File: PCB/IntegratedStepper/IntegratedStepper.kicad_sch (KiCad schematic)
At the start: 0 parts

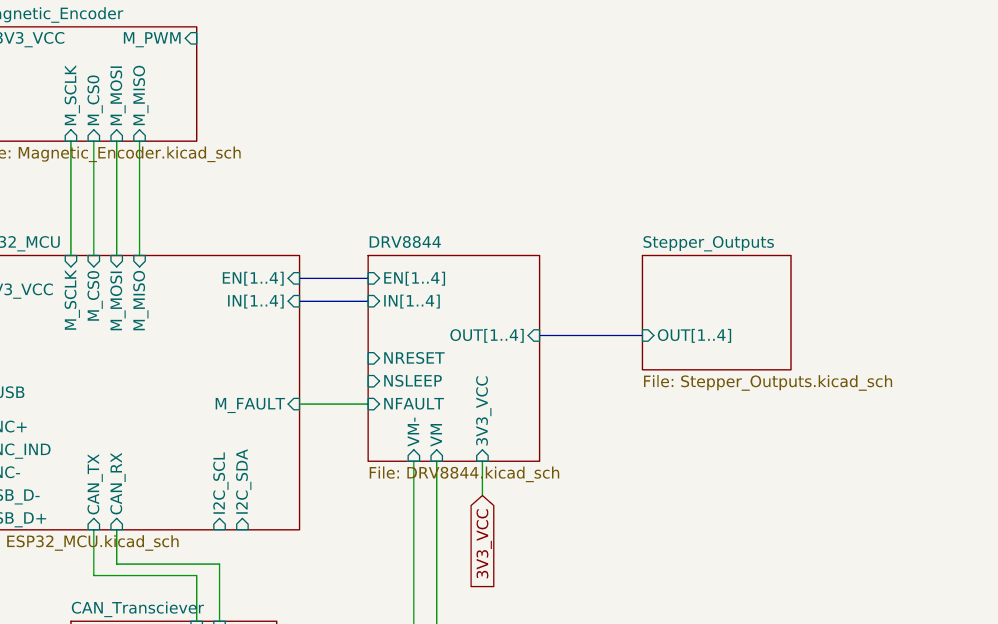
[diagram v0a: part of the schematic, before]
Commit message: Update PCB with DRV8243 for 12A capacity
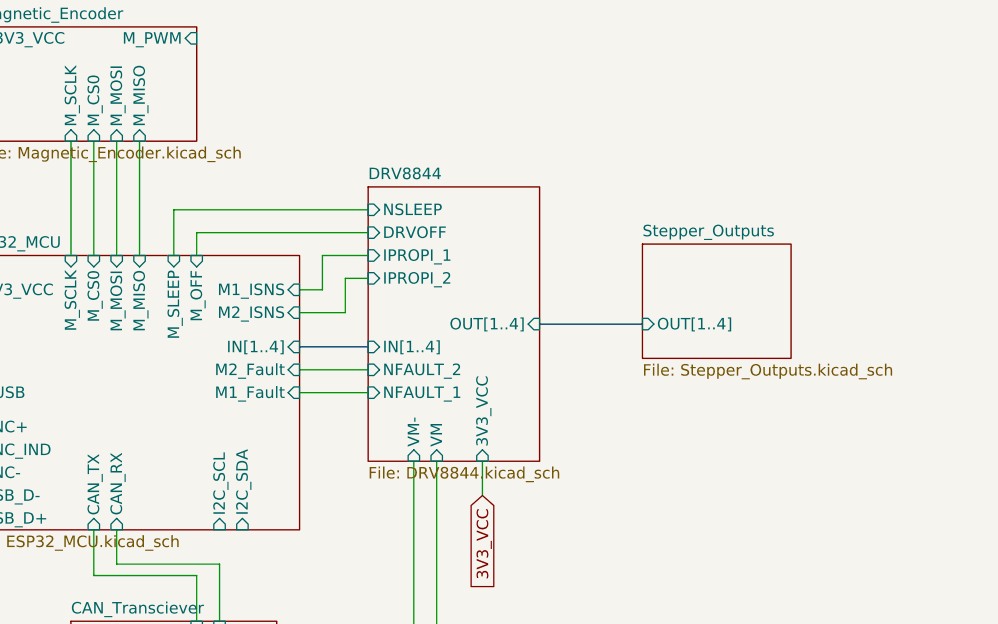
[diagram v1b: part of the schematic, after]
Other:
- sheet DRV8844 ports: added DRVOFF, IPROPI_1, IPROPI_2, NFAULT_1, NFAULT_2; removed EN[1..4], NFAULT, NRESET
- sheet ESP32_MCU ports: added M1_Fault, M1_ISNS, M2_Fault, M2_ISNS, M_OFF, M_SLEEP; removed EN[1..4], M_FAULT

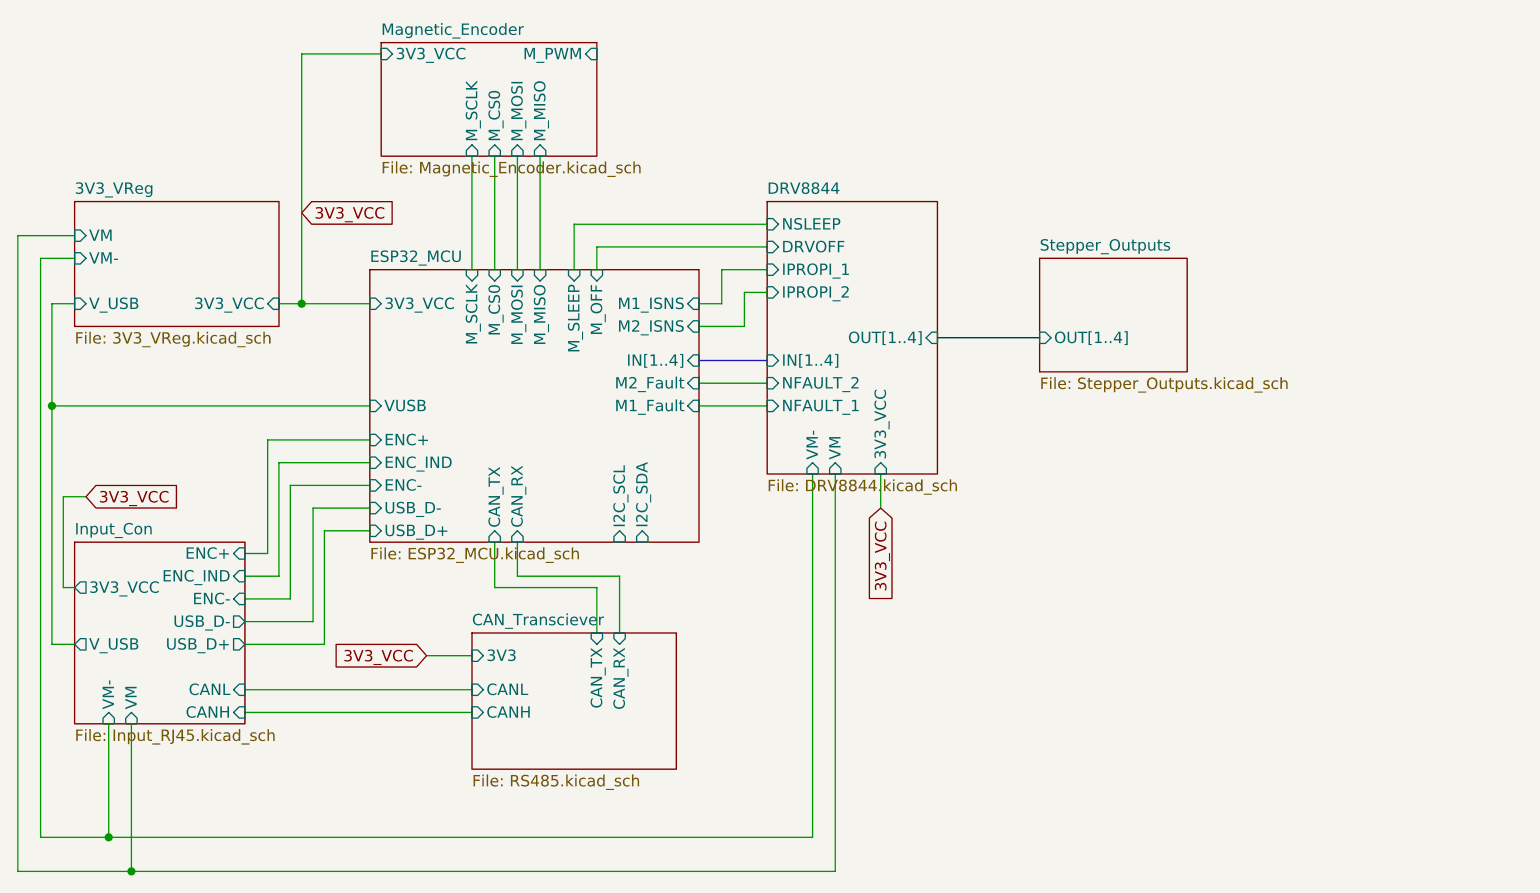
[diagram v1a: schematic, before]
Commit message: update new tester board sch
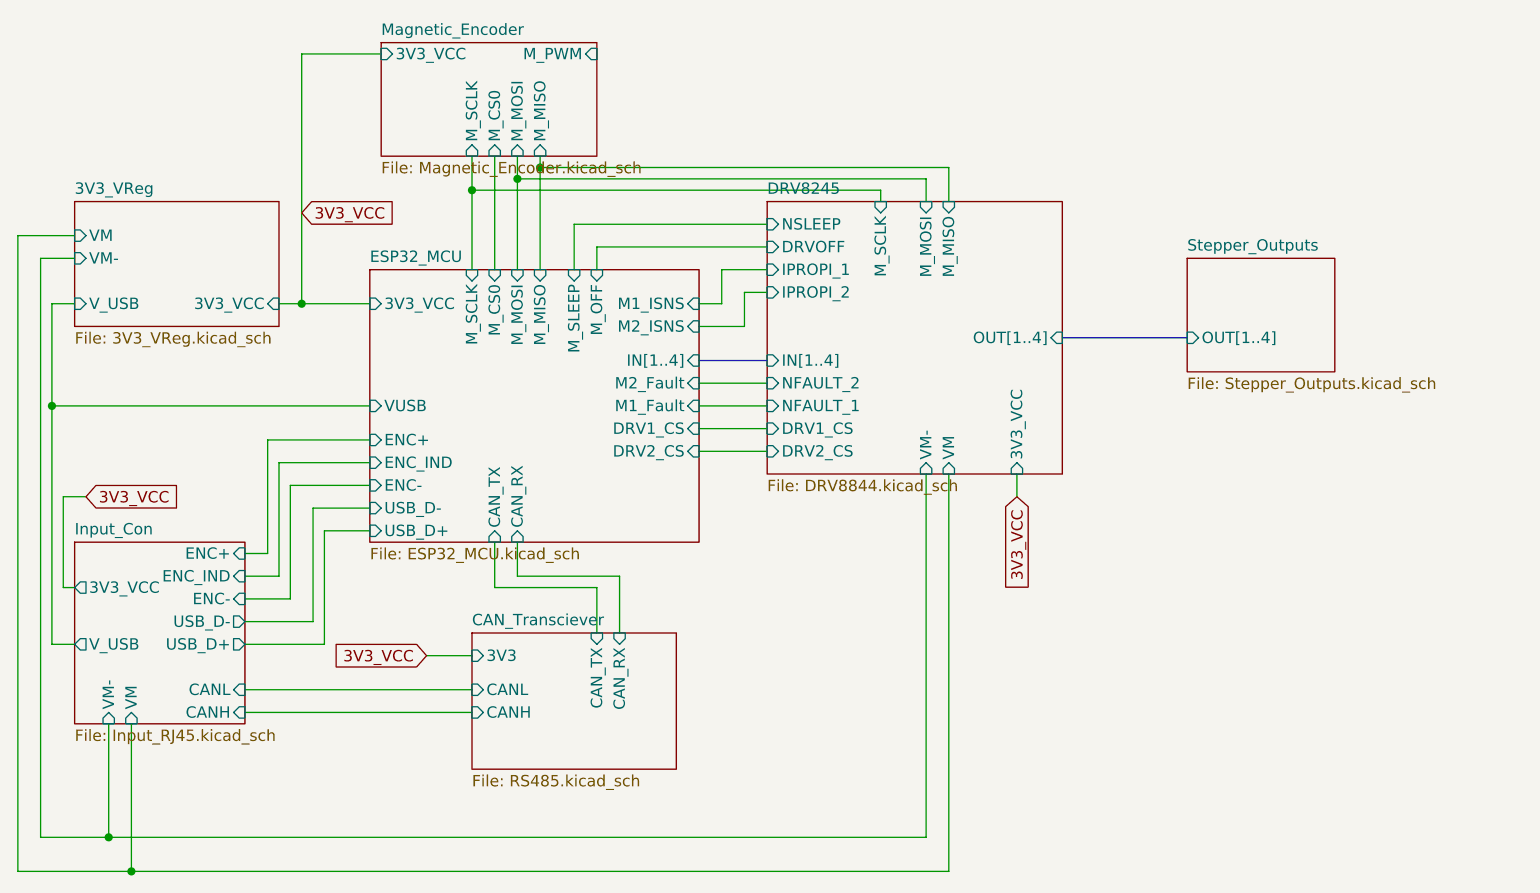
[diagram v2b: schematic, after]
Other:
- sheet DRV8844 renamed DRV8245
- sheet DRV8245 ports: added DRV1_CS, DRV2_CS, M_MISO, M_MOSI, M_SCLK; removed none
- sheet ESP32_MCU ports: added DRV1_CS, DRV2_CS; removed I2C_SCL, I2C_SDA
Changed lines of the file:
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@@
 	(paper "A4")
+	(junction
+		(at 123.19 59.69)
+		(diameter 0)
+		(color 0 0 0 0)
+	)
+	(junction
+		(at 115.57 62.23)
+		(diameter 0)
+		(color 0 0 0 0)
+	)
 	(junction
 		(at 77.47 138.43)
@@
 	)
 	(junction
+		(at 120.65 60.96)
+		(diameter 0)
+		(color 0 0 0 0)
+	)
+	(junction
 		(at 96.52 74.93)
 		(diameter 0)
@@
 	(wire
 		(pts
+			(xy 115.57 62.23) (xy 161.29 62.23)
+		)
+		(stroke
+			(width 0)
+			(type default)
+		)
+	)
+	(wire
+		(pts
 			(xy 129.54 68.58) (xy 148.59 68.58)
 		)
@@
 	(wire
 		(pts
+			(xy 120.65 58.42) (xy 120.65 60.96)
+		)
+		(stroke
+			(width 0)
+			(type default)
+		)
+	)
+	(wire
+		(pts
+			(xy 166.37 60.96) (xy 120.65 60.96)
+		)
+		(stroke
+			(width 0)
+			(type default)
+		)
+	)
+	(wire
+		(pts
 			(xy 93.98 74.93) (xy 96.52 74.93)
 		)
@@
 	(wire
 		(pts
-			(xy 123.19 58.42) (xy 123.19 71.12)
+			(xy 123.19 58.42) (xy 123.19 59.69)
 		)
 		(stroke
@@
 	(wire
 		(pts
+			(xy 140.97 91.44) (xy 148.59 91.44)
+		)
+		(stroke
+			(width 0)
+			(type default)
+		)
+	)
+	(wire
+		(pts
 			(xy 143.51 71.12) (xy 148.59 71.12)
 		)
@@
 	(wire
 		(pts
-			(xy 77.47 138.43) (xy 156.21 138.43)
+			(xy 77.47 138.43) (xy 168.91 138.43)
+		)
+		(stroke
+			(width 0)
+			(type default)
+		)
+	)
+	(wire
+		(pts
+			(xy 168.91 59.69) (xy 123.19 59.69)
 		)
 		(stroke
@@
 		)
 	)
-	(wire
-		(pts
-			(xy 115.57 58.42) (xy 115.57 71.12)
-		)
-		(stroke
-			(width 0)
-			(type default)
-		)
-	)
 	(bus
 		(pts
-			(xy 167.64 78.74) (xy 179.07 78.74)
+			(xy 181.61 78.74) (xy 195.58 78.74)
+		)
+		(stroke
+			(width 0)
+			(type default)
+		)
+	)
+	(wire
+		(pts
+			(xy 115.57 58.42) (xy 115.57 62.23)
 		)
 		(stroke
@@
 	(wire
 		(pts
+			(xy 115.57 62.23) (xy 115.57 71.12)
+		)
+		(stroke
+			(width 0)
+			(type default)
+		)
+	)
+	(wire
+		(pts
 			(xy 68.58 86.36) (xy 68.58 113.03)
 		)
@@
 	(wire
 		(pts
+			(xy 120.65 60.96) (xy 120.65 71.12)
+		)
+		(stroke
+			(width 0)
+			(type default)
+		)
+	)
+	(wire
+		(pts
 			(xy 104.14 92.71) (xy 93.98 92.71)
 		)
@@
 	(wire
 		(pts
-			(xy 153.67 134.62) (xy 153.67 93.98)
+			(xy 166.37 134.62) (xy 166.37 93.98)
 		)
 		(stroke
@@
 	(wire
 		(pts
-			(xy 74.93 134.62) (xy 153.67 134.62)
+			(xy 161.29 62.23) (xy 161.29 63.5)
+		)
+		(stroke
+			(width 0)
+			(type default)
+		)
+	)
+	(wire
+		(pts
+			(xy 140.97 88.9) (xy 148.59 88.9)
+		)
+		(stroke
+			(width 0)
+			(type default)
+		)
+	)
+	(wire
+		(pts
+			(xy 74.93 134.62) (xy 166.37 134.62)
 		)
 		(stroke
@@
 	(wire
 		(pts
-			(xy 156.21 138.43) (xy 156.21 93.98)
-		)
-		(stroke
-			(width 0)
-			(type default)
-		)
-	)
-	(wire
-		(pts
-			(xy 161.29 93.98) (xy 161.29 97.79)
+			(xy 168.91 138.43) (xy 168.91 93.98)
+		)
+		(stroke
+			(width 0)
+			(type default)
+		)
+	)
+	(wire
+		(pts
+			(xy 176.53 93.98) (xy 176.53 96.52)
 		)
 		(stroke
@@
 	(wire
 		(pts
+			(xy 168.91 63.5) (xy 168.91 59.69)
+		)
+		(stroke
+			(width 0)
+			(type default)
+		)
+	)
+	(wire
+		(pts
 			(xy 93.98 105.41) (xy 90.17 105.41)
 		)
@@
 	(wire
 		(pts
-			(xy 120.65 58.42) (xy 120.65 71.12)
+			(xy 123.19 59.69) (xy 123.19 71.12)
+		)
+		(stroke
+			(width 0)
+			(type default)
+		)
+	)
+	(wire
+		(pts
+			(xy 166.37 63.5) (xy 166.37 60.96)
 		)
 		(stroke
@@
 	(global_label "3V3_VCC"
 		(shape input)
-		(at 161.29 97.79 270)
+		(at 176.53 96.52 270)
 		(fields_autoplaced yes)
 		(effects
@@
 		)
 		(property "Intersheetrefs" "${INTERSHEET_REFS}"
-			(at 161.29 108.879 90)
+			(at 176.53 107.609 90)
 			(effects
 				(font
@@
 	)
 	(sheet
-		(at 179.07 69.85)
+		(at 195.58 69.85)
 		(size 16.51 12.7)
 		(fields_autoplaced yes)
@@
 		)
 		(property "Sheetname" "Stepper_Outputs"
-			(at 179.07 69.1384 0)
+			(at 195.58 69.1384 0)
 			(effects
 				(font
@@
 		)
 		(property "Sheetfile" "Stepper_Outputs.kicad_sch"
-			(at 179.07 83.1346 0)
+			(at 195.58 83.1346 0)
 			(effects
 				(font
@@
 		)
 		(pin "OUT[1..4]" input
-			(at 179.07 78.74 180)
+			(at 195.58 78.74 180)
 			(effects
 				(font
@@
 	(sheet
 		(at 148.59 63.5)
-		(size 19.05 30.48)
+		(size 33.02 30.48)
 		(fields_autoplaced yes)
 		(stroke
@@
 			(color 0 0 0 0.0000)
 		)
-		(property "Sheetname" "DRV8844"
+		(property "Sheetname" "DRV8245"
 			(at 148.59 62.7884 0)
 			(effects
@@
 		)
 		(pin "VM-" input
-			(at 153.67 93.98 270)
+			(at 166.37 93.98 270)
 			(effects
 				(font
@@
 		)
 		(pin "VM" input
-			(at 156.21 93.98 270)
+			(at 168.91 93.98 270)
 			(effects
 				(font
@@
 		)
 		(pin "OUT[1..4]" input
-			(at 167.64 78.74 0)
+			(at 181.61 78.74 0)
 			(effects
 				(font
@@
 		)
 		(pin "3V3_VCC" input
-			(at 161.29 93.98 270)
+			(at 176.53 93.98 270)
 			(effects
 				(font
@@
 		(pin "DRVOFF" input
 			(at 148.59 68.58 180)
+			(effects
+				(font
+					(size 1.27 1.27)
+				)
+				(justify left)
+			)
+		)
+		(pin "M_SCLK" input
+			(at 161.29 63.5 90)
+			(effects
+				(font
+					(size 1.27 1.27)
+				)
+				(justify right)
+			)
+		)
+		(pin "M_MISO" input
+			(at 168.91 63.5 90)
+			(effects
+				(font
+					(size 1.27 1.27)
+				)
+				(justify right)
+			)
+		)
+		(pin "M_MOSI" input
+			(at 166.37 63.5 90)
+			(effects
+				(font
+					(size 1.27 1.27)
+				)
+				(justify right)
+			)
+		)
+		(pin "DRV1_CS" input
+			(at 148.59 88.9 180)
+			(effects
+				(font
+					(size 1.27 1.27)
+				)
+				(justify left)
+			)
+		)
+		(pin "DRV2_CS" input
+			(at 148.59 91.44 180)
 			(effects
 				(font
@@
 			)
 		)
-		(pin "I2C_SCL" input
-			(at 132.08 101.6 270)
-			(effects
-				(font
-					(size 1.27 1.27)
-				)
-				(justify left)
-			)
-		)
 		(pin "ENC+" input
 			(at 104.14 90.17 180)
@@
 			)
 		)
-		(pin "I2C_SDA" input
-			(at 134.62 101.6 270)
-			(effects
-				(font
-					(size 1.27 1.27)
-				)
-				(justify left)
-			)
-		)
 		(pin "ENC-" input
 			(at 104.14 95.25 180)
@@
 			(effects
 				(font
+					(size 1.27 1.27)
+				)
+				(justify right)
+			)
+		)
+		(pin "DRV1_CS" input
+			(at 140.97 88.9 0)
+			(effects
+				(font
+					(size 1.27 1.27)
+				)
+				(justify right)
+			)
+		)
+		(pin "DRV2_CS" input
+			(at 140.97 91.44 0)
+			(effects
+				(font
